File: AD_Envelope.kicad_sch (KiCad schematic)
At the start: 91 parts, among them Q15 MMBT3906LT1G, Q18 MMBT3906LT1G, SW14 SW_SPST, SW15 SW_Push, SW16 SW_SPST, SW17 SW_SPDT, SW18 SW_SPDT, SW19 SW_Push, SW20 SW_DPST, SW21 SW_DPST, SW22 SW_SPST, SW23 SW_SPST, U13 TL072, U14 TL072, U15 TL074

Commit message: more work...
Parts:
- C68, C69, C73, C74, C75, C76, C77, C78, C79, C80, C81: footprint Capacitor_SMD:C_0805_2012Metric_Pad1.18x1.45mm_HandSolder -> Capacitor_SMD:C_0805_2012Metric
- C70, C71: value 2.2nf -> 2.2nF; footprint Capacitor_SMD:C_0805_2012Metric_Pad1.18x1.45mm_HandSolder -> Capacitor_SMD:C_0603_1608Metric
- C72, C82, C83: footprint Capacitor_SMD:C_0805_2012Metric_Pad1.18x1.45mm_HandSolder -> Capacitor_SMD:C_0603_1608Metric
- R134, R135, R136, R137, R138, R139, R140, R141, R142, R143, R144, R145, R146, R147, R148, R149, R150, R151, R152, R153, R154, R155, R156, R157, R158, R159, R160, R161: footprint Resistor_SMD:R_0805_2012Metric_Pad1.20x1.40mm_HandSolder -> Resistor_SMD:R_0603_1608Metric

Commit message: finishing schematic 1.0
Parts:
- SW14, SW16, SW22, SW23: footprint (none) -> SynthProjConnectors:MTS-103-A01-T0
- SW15, SW19: footprint (none) -> Button_Switch_THT:SW_PUSH_6mm_H13mm
- SW17, SW18: footprint SynthProjConnectors:ST-0-102-A01-T000-LF -> SynthProjConnectors:MTS-103-A01-T0
- SW20, SW21: footprint (none) -> SynthProjConnectors:MTS-203-A1-T0
- renumbered C68 to C69, C69 to C70, C70 to C71, C71 to C72, C72 to C73, C73 to C74, C74 to C75, C75 to C76, C76 to C77, C77 to C78, C78 to C79, C79 to C80, C80 to C81, C81 to C82, C82 to C83, C83 to C84
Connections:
- net X54: now also SW21.2; no longer SW21.3
- net X55: now also SW21.1; no longer SW21.2
- net X59: now also SW21.5; no longer SW21.1
- net at C72.1, D18.1 (K), R146.2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: now also SW20.1; no longer SW20.2
- net at C72.2, Q?.2 (S), R144.2: now also SW20.5; no longer SW20.1
- net at R141.1: now also SW20.2; no longer SW20.3

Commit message: Doing some layout
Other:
- note added: "Off"
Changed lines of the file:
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@@
+    (effects (font (size 1.27 1.27)) (justify left bottom))
+  )
+  (text "Volume" (at 234.315 49.53 0)
     (effects (font (size 1.27 1.27)) (justify left bottom))
   )
   (text "Gate" (at 105.41 138.43 0)
+    (effects (font (size 1.27 1.27)) (justify left bottom))
+  )
+  (text "Off" (at 50.165 123.19 0)
     (effects (font (size 1.27 1.27)) (justify left bottom))
   )
@@
     (effects (font (size 1.27 1.27)) (justify left bottom))
   )
+  (text "Attack" (at 192.405 24.13 0)
+    (effects (font (size 1.27 1.27)) (justify left bottom))
+  )
+  (text "Decay" (at 192.405 43.18 0)
+    (effects (font (size 1.27 1.27)) (justify left bottom))
+  )
+  (text "Repeat" (at 50.165 125.73 0)
+    (effects (font (size 1.27 1.27)) (justify left bottom))
+  )
   (text "Gate Ind" (at 186.69 82.55 0)
     (effects (font (size 1.27 1.27)) (justify left bottom))
@@
     (effects (font (size 1.27 1.27)) (justify left bottom))
   )
+  (text "Off" (at 43.18 83.82 0)
+    (effects (font (size 1.27 1.27)) (justify left bottom))
+  )
+  (text "S&H" (at 50.165 120.65 0)
+    (effects (font (size 1.27 1.27)) (justify left bottom))
+  )

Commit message: routing work...
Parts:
- removed U13: TL072, Package_SO:SOP-8_3.9x4.9mm_P1.27mm, symbol Amplifier_Operational:TL072
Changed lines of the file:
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@@
     (effects (font (size 1.27 1.27)) (justify left))
-  )
-  (symbol (lib_id "Amplifier_Operational:TL072") (at 218.44 88.9 0) (unit 3)
-    (in_bom yes) (on_board yes) (dnp no)
-    (property "Reference" "U13" (at 217.3732 87.7316 0)
-      (effects (font (size 1.27 1.27)) (justify left))
-    )
-    (property "Value" "TL072" (at 217.3732 90.043 0)
-      (effects (font (size 1.27 1.27)) (justify left))
-    )
-    (property "Footprint" "Package_SO:SOP-8_3.9x4.9mm_P1.27mm" (at 218.44 88.9 0)
-      (effects (font (size 1.27 1.27)) hide)
-    )
-    (property "Datasheet" "http://www.ti.com/lit/ds/symlink/tl071.pdf" (at 218.44 88.9 0)
-      (effects (font (size 1.27 1.27)) hide)
-    )
-    (pin "8")
-    (pin "2")
-    (pin "5")
-    (pin "6")
-    (pin "7")
-    (pin "4")
-    (pin "1")
-    (pin "3")
-    (instances
-      (project "SynthProj"
-        (path "/9021c97e-351f-4ed9-b393-50257df6a463/00000000-0000-0000-0000-00006620617f"
-          (reference "U13") (unit 3)
-        )
-        (path "/9021c97e-351f-4ed9-b393-50257df6a463/00000000-0000-0000-0000-0000659a4e2e"
-          (reference "U?") (unit 3)
-        )
-      )
-    )
-  )
-  (symbol (lib_id "power:+12V") (at 215.9 81.28 0) (unit 1)
-    (in_bom yes) (on_board yes) (dnp no)
-    (property "Reference" "#PWR0199" (at 215.9 85.09 0)
-      (effects (font (size 1.27 1.27)) hide)
-    )
-    (property "Value" "+12V" (at 216.281 76.8858 0)
-      (effects (font (size 1.27 1.27)))
-    )
-    (property "Footprint" "" (at 215.9 81.28 0)
-      (effects (font (size 1.27 1.27)) hide)
-    )
-    (property "Datasheet" "" (at 215.9 81.28 0)
-      (effects (font (size 1.27 1.27)) hide)
-    )
-    (pin "1")
-    (instances
-      (project "SynthProj"
-        (path "/9021c97e-351f-4ed9-b393-50257df6a463/00000000-0000-0000-0000-00006620617f"
-          (reference "#PWR0199") (unit 1)
-        )
-        (path "/9021c97e-351f-4ed9-b393-50257df6a463/00000000-0000-0000-0000-0000659a4e2e"
-          (reference "#PWR?") (unit 1)
-        )
-      )
-    )
   )
   (symbol (lib_id "power:+12V") (at 223.52 81.28 0) (unit 1)
@@
         )
         (path "/9021c97e-351f-4ed9-b393-50257df6a463/00000000-0000-0000-0000-0000659a4e2e"
-          (reference "#PWR?") (unit 1)
-        )
-      )
-    )
-  )
-  (symbol (lib_id "power:-12V") (at 215.9 96.52 180) (unit 1)
-    (in_bom yes) (on_board yes) (dnp no)
-    (property "Reference" "#PWR0200" (at 215.9 99.06 0)
-      (effects (font (size 1.27 1.27)) hide)
-    )
-    (property "Value" "-12V" (at 215.519 100.9142 0)
-      (effects (font (size 1.27 1.27)))
-    )
-    (property "Footprint" "" (at 215.9 96.52 0)
-      (effects (font (size 1.27 1.27)) hide)
-    )
-    (property "Datasheet" "" (at 215.9 96.52 0)
-      (effects (font (size 1.27 1.27)) hide)
-    )
-    (pin "1")
-    (instances
-      (project "SynthProj"
-        (path "/9021c97e-351f-4ed9-b393-50257df6a463/00000000-0000-0000-0000-00006620617f"
-          (reference "#PWR0200") (unit 1)
-        )
-        (path "/9021c97e-351f-4ed9-b393-50257df6a463/00000000-0000-0000-0000-0000659a4e2e"

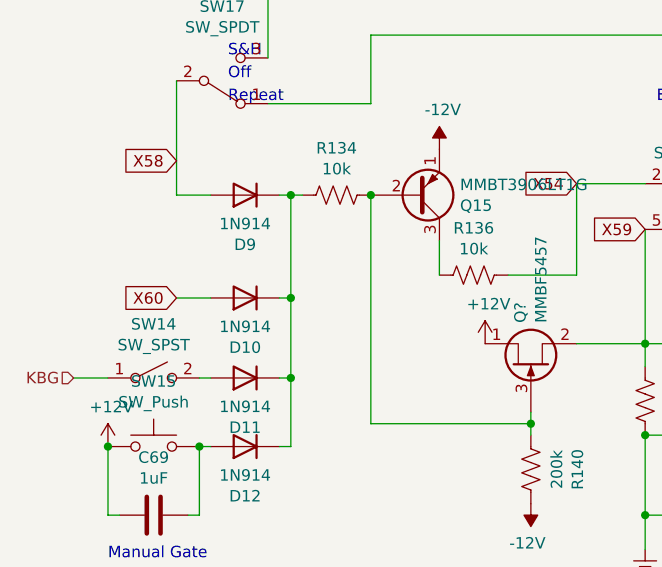
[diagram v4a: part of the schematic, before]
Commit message: lots of routes, added vco3, lfo2.
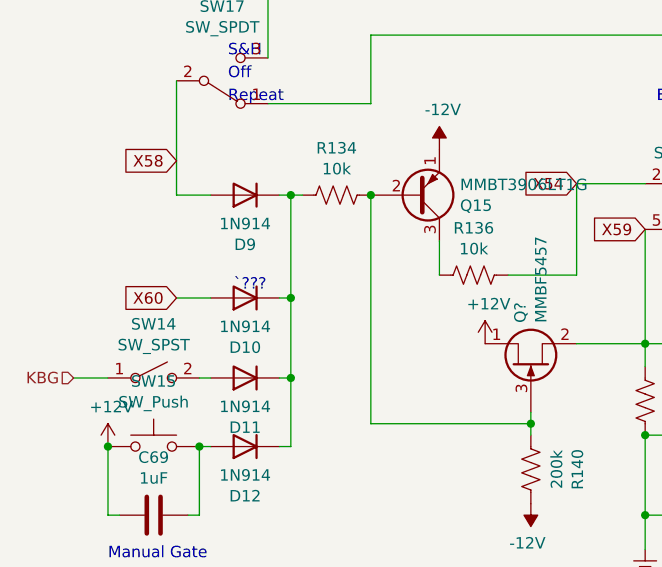
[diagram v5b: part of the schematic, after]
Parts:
- SW14, SW16, SW17, SW18, SW22, SW23: footprint SynthProjConnectors:MTS-103-A01-T0 -> SynthProjConnectors:SMTS-102
- SW20, SW21: footprint SynthProjConnectors:MTS-203-A1-T0 -> SynthProjConnectors:SMTS-202
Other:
- note added: "`???"
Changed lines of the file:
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@@
     (effects (font (size 1.27 1.27)) (justify left bottom))
   )
+  (text "`???" (at 50.8 146.685 0)
+    (effects (font (size 1.27 1.27)) (justify left bottom))
+  )
   (text "EG Mode" (at 96.52 21.59 0)
     (effects (font (size 1.27 1.27)) (justify left bottom))
@@
       (effects (font (size 1.27 1.27)) (justify left))
     )
-    (property "Footprint" "SynthProjConnectors:MTS-103-A01-T0" (at 43.18 40.64 0)
+    (property "Footprint" "SynthProjConnectors:SMTS-102" (at 43.18 40.64 0)
       (effects (font (size 1.27 1.27)) hide)
     )
@@
       (effects (font (size 1.27 1.27)))
     )
-    (property "Footprint" "SynthProjConnectors:MTS-203-A1-T0" (at 100.33 31.75 0)
+    (property "Footprint" "SynthProjConnectors:SMTS-202" (at 100.33 31.75 0)
       (effects (font (size 1.27 1.27)) hide)
     )
@@
       (effects (font (size 1.27 1.27)))
     )
-    (property "Footprint" "SynthProjConnectors:MTS-103-A01-T0" (at 220.98 26.67 0)
+    (property "Footprint" "SynthProjConnectors:SMTS-102" (at 220.98 26.67 0)
       (effects (font (size 1.27 1.27)) hide)
     )
@@
       (effects (font (size 1.27 1.27)))
     )
-    (property "Footprint" "SynthProjConnectors:MTS-103-A01-T0" (at 50.8 83.82 0)
+    (property "Footprint" "SynthProjConnectors:SMTS-102" (at 50.8 83.82 0)
       (effects (font (size 1.27 1.27)) hide)
     )
@@
       (effects (font (size 1.27 1.27)))
     )
-    (property "Footprint" "SynthProjConnectors:MTS-103-A01-T0" (at 49.53 123.19 0)
+    (property "Footprint" "SynthProjConnectors:SMTS-102" (at 49.53 123.19 0)
       (effects (font (size 1.27 1.27)) hide)
     )
@@
       (effects (font (size 1.27 1.27)))
     )
-    (property "Footprint" "SynthProjConnectors:MTS-103-A01-T0" (at 41.91 156.21 0)
+    (property "Footprint" "SynthProjConnectors:SMTS-102" (at 41.91 156.21 0)
       (effects (font (size 1.27 1.27)) hide)
     )
@@
       (effects (font (size 1.27 1.27)))
     )
-    (property "Footprint" "SynthProjConnectors:MTS-103-A01-T0" (at 215.9 123.19 0)
+    (property "Footprint" "SynthProjConnectors:SMTS-102" (at 215.9 123.19 0)
       (effects (font (size 1.27 1.27)) hide)
     )
@@
       (effects (font (size 1.27 1.27)))
     )
-    (property "Footprint" "SynthProjConnectors:MTS-203-A1-T0" (at 101.6 137.16 0)
+    (property "Footprint" "SynthProjConnectors:SMTS-202" (at 101.6 137.16 0)
       (effects (font (size 1.27 1.27)) hide)
     )

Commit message: more and more routing
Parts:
- removed D10: 1N914, Diode_SMD:D_SOD-323F, symbol Diode:1N914
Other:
- note removed: "`???"
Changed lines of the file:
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@@
   (junction (at 171.45 33.02) (diameter 0) (color 0 0 0 0)
   )
-  (junction (at 57.15 147.32) (diameter 0) (color 0 0 0 0)
-  )
   (junction (at 142.24 45.72) (diameter 0) (color 0 0 0 0)
   )
@@
     (stroke (width 0) (type default))
   )
-  (wire (pts (xy 44.45 147.32) (xy 48.26 147.32))
-    (stroke (width 0) (type default))
-  )
   (wire (pts (xy 204.47 26.67) (xy 200.66 26.67))
     (stroke (width 0) (type default))
@@
     (stroke (width 0) (type default))
   )
-  (wire (pts (xy 57.15 135.89) (xy 57.15 147.32))
+  (wire (pts (xy 57.15 135.89) (xy 57.15 156.21))
     (stroke (width 0) (type default))
   )
@@
     (stroke (width 0) (type default))
   )
-  (wire (pts (xy 55.88 147.32) (xy 57.15 147.32))
-    (stroke (width 0) (type default))
-  )
   (wire (pts (xy 142.24 45.72) (xy 142.24 50.8))
     (stroke (width 0) (type default))
@@
     (stroke (width 0) (type default))
   )
-  (wire (pts (xy 57.15 147.32) (xy 57.15 156.21))
-    (stroke (width 0) (type default))
-  )
   (wire (pts (xy 128.27 53.34) (xy 132.08 53.34))
     (stroke (width 0) (type default))
@@
     (effects (font (size 1.27 1.27)) (justify left bottom))
   )
-  (text "`???" (at 50.8 146.685 0)
-    (effects (font (size 1.27 1.27)) (justify left bottom))
-  )
   (text "EG Mode" (at 96.52 21.59 0)
     (effects (font (size 1.27 1.27)) (justify left bottom))
@@
     )
   )
-  (global_label "X60" (shape input) (at 44.45 147.32 180) (fields_autoplaced)
-    (effects (font (size 1.27 1.27)) (justify right))
-    (property "Intersheetrefs" "${INTERSHEET_REFS}" (at 37.8363 147.32 0)
-      (effects (font (size 1.27 1.27)) (justify right) hide)
-    )
-  )
   (global_label "X48" (shape input) (at 185.42 33.02 90)
     (effects (font (size 1.27 1.27)) (justify left))
@@
         )
       )
-    )
-  )
-  (symbol (lib_id "Diode:1N914") (at 52.07 147.32 180) (unit 1)
-    (in_bom yes) (on_board yes) (dnp no)
-    (property "Reference" "D10" (at 52.07 152.8318 0)
-      (effects (font (size 1.27 1.27)))
-    )
-    (property "Value" "1N914" (at 52.07 150.5204 0)
-      (effects (font (size 1.27 1.27)))
-    )
-    (property "Footprint" "Diode_SMD:D_SOD-323F" (at 52.07 142.875 0)
-      (effects (font (size 1.27 1.27)) hide)
-    )
-    (property "Datasheet" "http://www.vishay.com/docs/85622/1n914.pdf" (at 52.07 147.32 0)
-      (effects (font (size 1.27 1.27)) hide)
-    )
-    (pin "1")
-    (pin "2")
-    (instances
-      (project "SynthProj"
-        (path "/9021c97e-351f-4ed9-b393-50257df6a463/00000000-0000-0000-0000-00006620617f"
-          (reference "D10") (unit 1)
-        )
-        (path "/9021c97e-351f-4ed9-b393-50257df6a463/00000000-0000-0000-0000-0000659a4e2e"
-          (reference "D?") (unit 1)
-        )
-      )

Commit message: more work
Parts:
- D19, D28: footprint LED_SMD:LED_0805_2012Metric -> LED_THT:LED_D3.0mm
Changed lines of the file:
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@@
       (effects (font (size 1.27 1.27)) (justify right))
     )
-    (property "Footprint" "LED_SMD:LED_0805_2012Metric" (at 118.11 90.17 0)
+    (property "Footprint" "LED_THT:LED_D3.0mm" (at 118.11 90.17 0)
       (effects (font (size 1.27 1.27)) hide)
     )
@@
       (effects (font (size 1.27 1.27)) (justify right))
     )
-    (property "Footprint" "LED_SMD:LED_0805_2012Metric" (at 190.5 93.98 0)
-      (effects (font (size 1.27 1.27)) hide)
-    )
+    (property "Footprint" "LED_THT:LED_D3.0mm" (at 190.5 93.98 0)
+      (effects (font (size 1.27 1.27)) hide)
+    )

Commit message: more and more and more and more and more routing
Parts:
- removed C79, C80: 4.7uF, Capacitor_SMD:C_0805_2012Metric, symbol Device:C
- removed C83, C84: 47nF, Capacitor_SMD:C_0603_1608Metric, symbol Device:C
- added C39, C40: 470nF, Capacitor_SMD:C_0805_2012Metric, symbol Device:C
- added unit 3 of U14
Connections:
- net +12V: now also C40.2, U14.8 (V+)
- net -12V: now also C39.1, U14.4 (V-)
- net GNDREF: now also C39.2, C40.1
